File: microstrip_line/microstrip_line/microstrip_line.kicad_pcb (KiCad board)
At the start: 2 copper layers, 30 x 16 mm, 0 parts

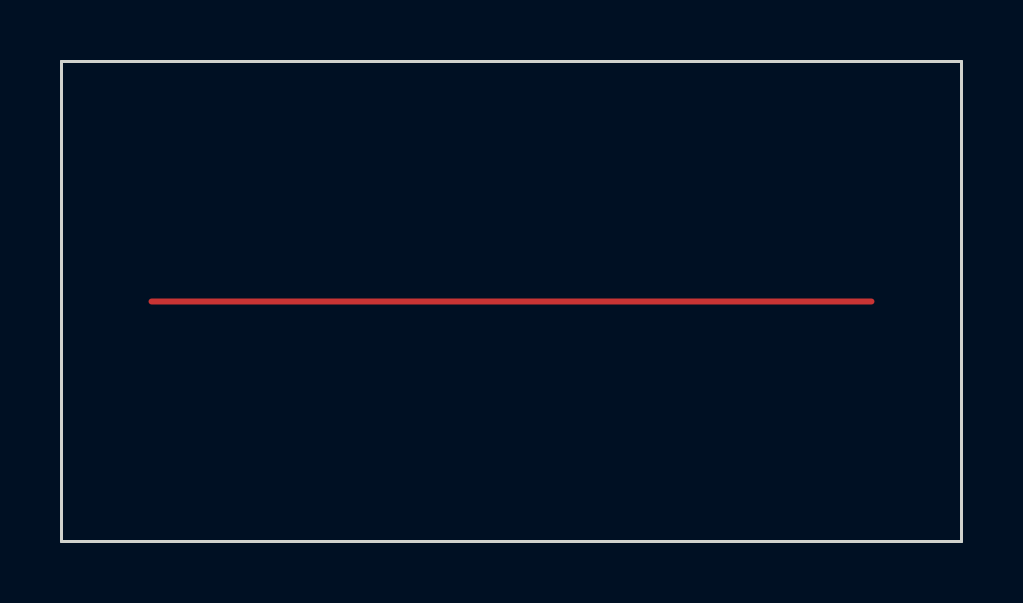
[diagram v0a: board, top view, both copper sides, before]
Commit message: Automatized PyBERT implementation
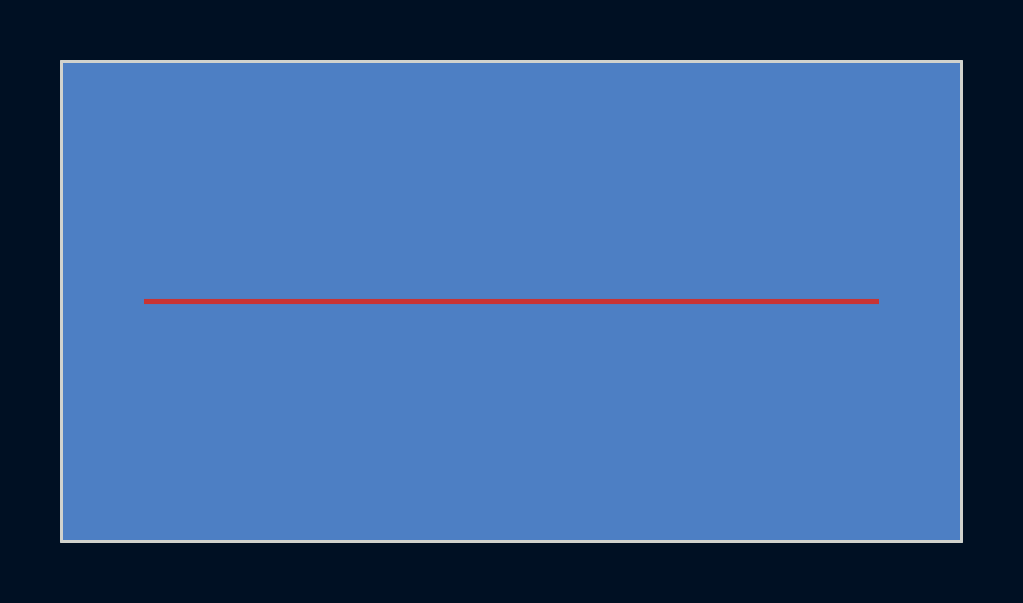
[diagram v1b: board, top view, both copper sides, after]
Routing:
- net (no net): track 24.0 -> 0.00 mm
- removed copper zone on B.Cu, net (none)
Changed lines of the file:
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@@
 	)
 	(setup
+		(stackup
+			(layer "F.SilkS"
+				(type "Top Silk Screen")
+			)
+			(layer "F.Paste"
+				(type "Top Solder Paste")
+			)
+			(layer "F.Mask"
+				(type "Top Solder Mask")
+				(thickness 0.01)
+			)
+			(layer "F.Cu"
+				(type "copper")
+				(thickness 0.035)
+			)
+			(layer "dielectric 1"
+				(type "core")
+				(thickness 1.51)
+				(material "FR4")
+				(epsilon_r 4.5)
+				(loss_tangent 0.02)
+			)
+			(layer "B.Cu"
+				(type "copper")
+				(thickness 0.035)
+			)
+			(layer "B.Mask"
+				(type "Bottom Solder Mask")
+				(thickness 0.01)
+			)
+			(layer "B.Paste"
+				(type "Bottom Solder Paste")
+			)
+			(layer "B.SilkS"
+				(type "Bottom Silk Screen")
+			)
+			(copper_finish "None")
+			(dielectric_constraints no)
+		)
 		(pad_to_mask_clearance 0)
 		(allow_soldermask_bridges_in_footprints no)
@@
 	)
 	(gr_rect
+		(start 144.75 97.915)
+		(end 169.25 98.085)
+		(stroke
+			(width 0)
+			(type solid)
+		)
+		(fill yes)
+		(layer "F.Cu")
+		(net "1")
+	)
+	(gr_rect
+		(start 142 90)
+		(end 172 106)
+		(stroke
+			(width 0)
+			(type default)
+		)
+		(fill yes)
+		(layer "B.Cu")
+	)
+	(gr_rect
 		(start 142 90)
 		(end 172 106)
@@
 		(layer "Edge.Cuts")
 	)
-	(segment
-		(start 145 98)
-		(end 169 98)
-		(width 0.2)
-		(layer "F.Cu")
-		(net "")
-	)
-	(zone
-		(layer "B.Cu")
-		(hatch edge 0.5)
-		(connect_pads
-			(clearance 0.5)
+	(gr_line
+		(start 142.5 98)
+		(end 171.25 98)
+		(stroke
+			(width 0.1)
+			(type default)
 		)
-		(min_thickness 0.25)
-		(fill yes
-			(thermal_gap 0.5)
-			(thermal_bridge_width 0.5)
-			(island_removal_mode 1)
-		)
-		(polygon
-			(pts
-				(xy 142 106) (xy 142 90) (xy 172 90) (xy 172 106)
-			)
-		)
+		(layer "F.Fab")
 	)
 	(embedded_fonts no)

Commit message: Update microstrip simulation project
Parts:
- added SP1: Simulation_Port, Barsotion-Simulation-Ports:Simulation_Port, F.Cu at (146.0, 98.0)
- added SP2: Simulation_Port, Barsotion-Simulation-Ports:Simulation_Port, F.Cu at (168.0, 98.0)
